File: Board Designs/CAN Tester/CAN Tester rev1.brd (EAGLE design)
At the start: 160 x 100 mm, 0 parts

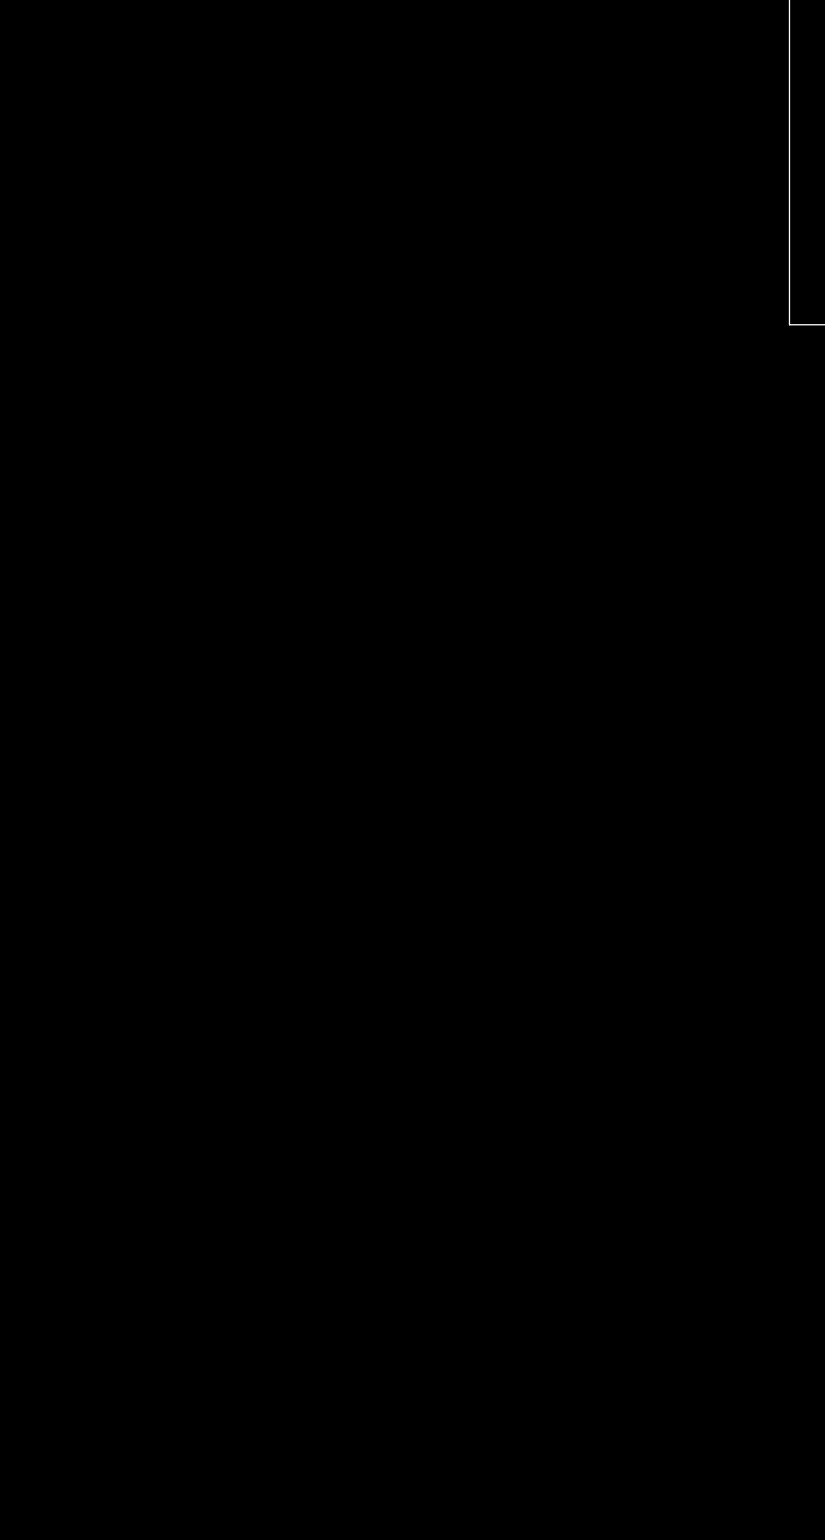
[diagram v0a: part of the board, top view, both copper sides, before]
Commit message: Added all parts to form can tester board
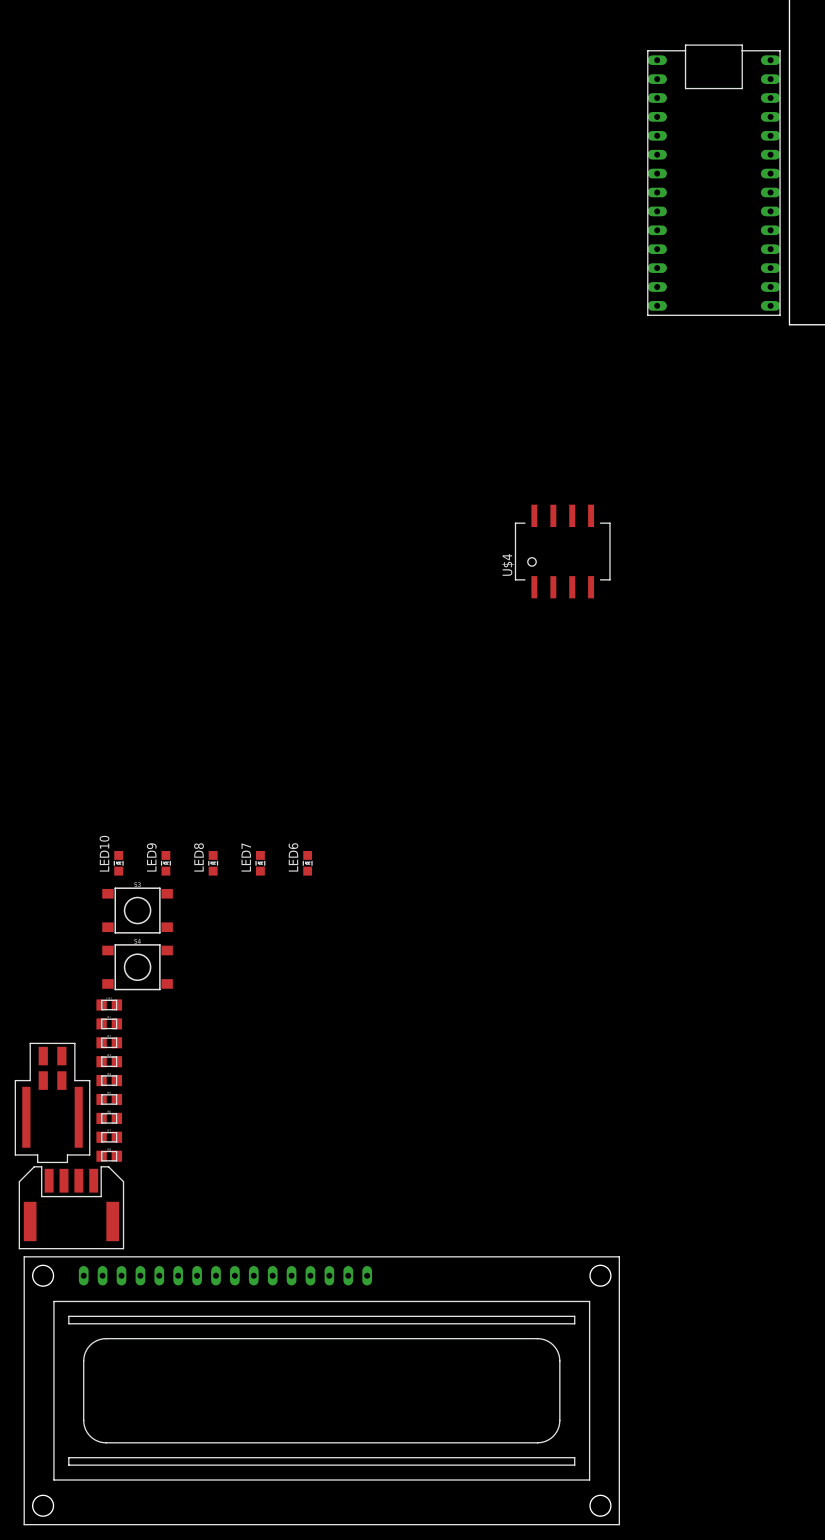
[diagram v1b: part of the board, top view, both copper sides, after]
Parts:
- added LED10, LED6, LED7, LED8, LED9: (no value), HyTechDevices:LED-805
- added R1: 120, HyTechDevices:0805
- added R2, R3, R4, R5, R6: 220, HyTechDevices:0805
- added R7, R8: 10K, HyTechDevices:0805
- added S3, S4: (no value), HyTechDevices:TACTILE_SWITCH_SMD_6.2MM_TALL
- added U$1: TEENSY_3.2_SIMPLE, HyTechDevices:TEENSY_3.2_SIMPLE
- added U$2: JUMPER, HyTechDevices:0805
- added U$4: ISO1050CAN, HyTechDevices:DUB8
- added X1: Minifit, HyTechDevices:DURACLIK_RIGHT_ANGLE-4
- added X2: HD44780LCD-1602, HyTechDevices:LCD1602
- added X3: Nanofit, HyTechDevices:NANO-FIT_RIGHT_ANGLE-4-SURFACE
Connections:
- new net N$1: R2.2, R3.1
- new net N$2: R3.2, R4.1
- new net N$3: LED10.A, R5.1

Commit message: increased component spacing
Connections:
- removed net N$1: R2.2, R3.1
- removed net N$2: R3.2, R4.1
- removed net N$3: LED10.A, R5.1
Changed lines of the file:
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@@
 </elements>
 <signals>
-<signal name="N$1">
-<contactref element="R2" pad="2"/>
-<contactref element="R3" pad="1"/>
-<wire x1="-90.415" y1="-96.52" x2="-92.465" y2="-99.06" width="0" layer="19" extent="1-1"/>
-</signal>
-<signal name="N$2">
-<contactref element="R3" pad="2"/>
-<contactref element="R4" pad="1"/>
-<wire x1="-90.415" y1="-99.06" x2="-92.465" y2="-101.6" width="0" layer="19" extent="1-1"/>
-</signal>
-<signal name="N$3">
-<contactref element="LED10" pad="A"/>
-<contactref element="R5" pad="1"/>
-<wire x1="-90.17" y1="-73.44" x2="-92.465" y2="-104.14" width="0" layer="19" extent="1-1"/>
-</signal>
 </signals>
 <mfgpreviewcolors>

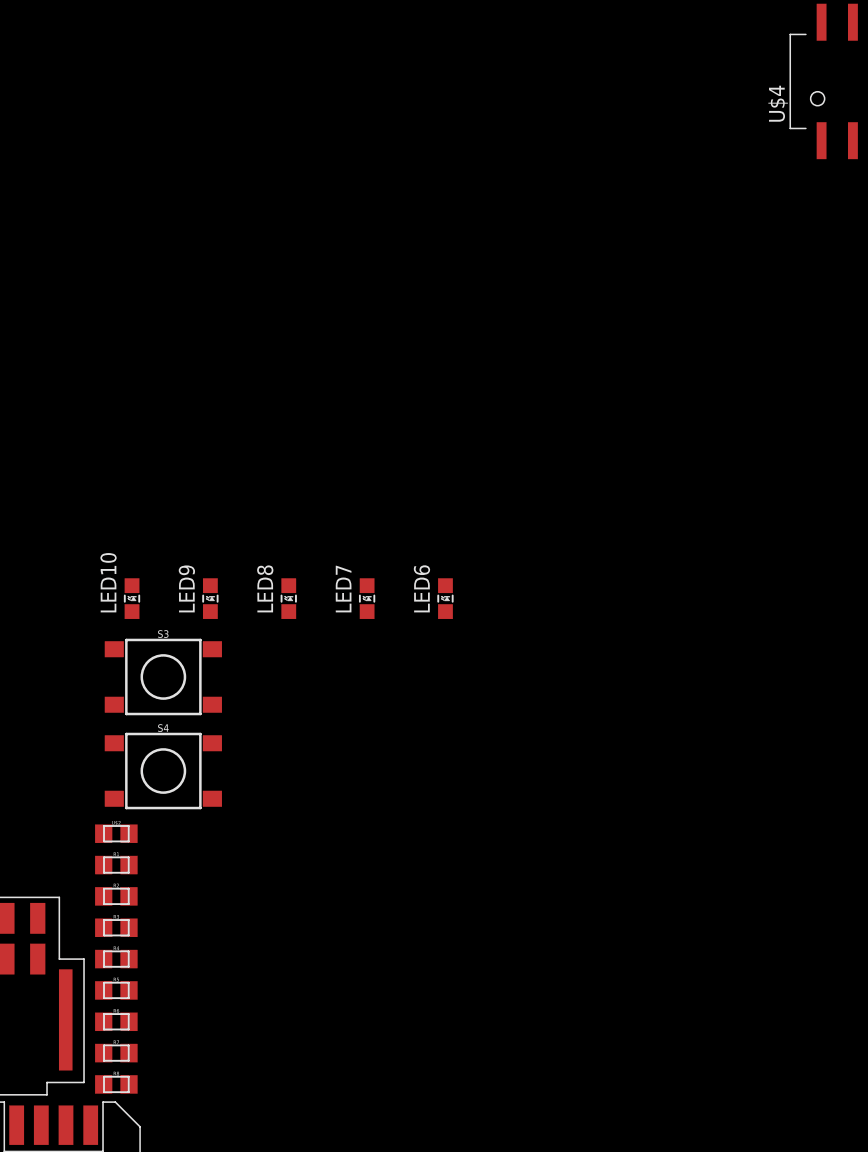
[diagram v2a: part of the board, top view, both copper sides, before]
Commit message: Labeled all componenets and organized them to make schematic later
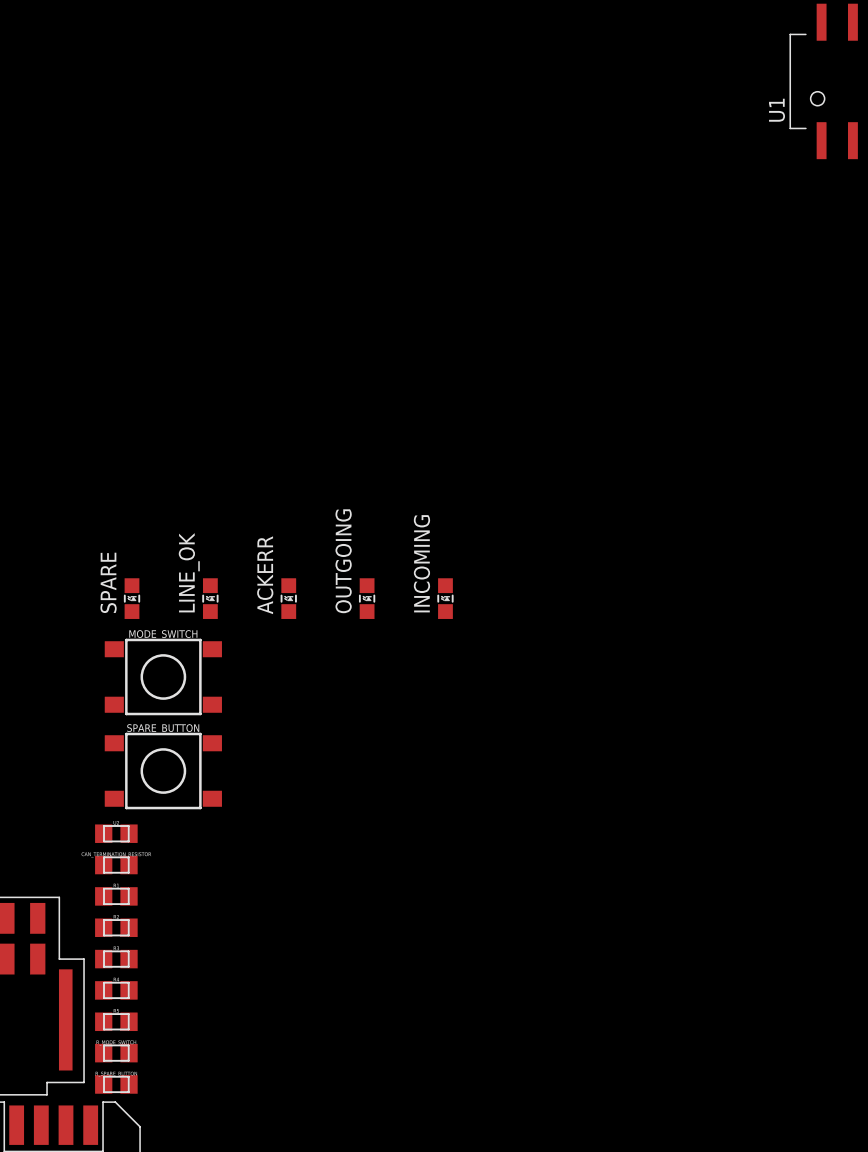
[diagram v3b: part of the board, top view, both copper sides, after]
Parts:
- removed R6: 220, HyTechDevices:0805
- added CAN_TERMINATION_RESISTOR: 120, HyTechDevices:0805
- ACKERR: value (none) -> RED
- INCOMING: value (none) -> YELLOW
- LINE_OK: value (none) -> GREEN
- OUTGOING: value (none) -> BLUE
- R1: value 120 -> 220
- SPARE: value (none) -> WHITE
- U1: value ISO1050CAN -> ISOLATED CAN TERMINAL
- U2: value JUMPER -> TERMINATION_RESISTOR_JUMPER
- U4: value HD44780LCD-1602 -> CHARACTER_LCD
- moved R2 2.54 mm to (-91.4, -99.1)
- moved R4 2.54 mm to (-91.4, -104.1)
- moved R5 2.54 mm to (-91.4, -106.7)
- moved R1 2.54 mm to (-91.4, -96.5)
- moved R3 2.54 mm to (-91.4, -101.6)
- renumbered LED10 to SPARE, LED6 to INCOMING, LED7 to OUTGOING, LED8 to ACKERR, LED9 to LINE_OK, R7 to R_MODE_SWITCH, R8 to R_SPARE_BUTTON, S3 to MODE_SWITCH, S4 to SPARE_BUTTON, U$1 to U3, U$2 to U2, U$4 to U1, X1 to M1, X2 to U4, X3 to M2
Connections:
- new net N$1: CAN_TERMINATION_RESISTOR.1, U2.2
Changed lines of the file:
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@@
 </autorouter>
 <elements>
-<element name="U$1" library="HyTechDevices" package="TEENSY_3.2_SIMPLE" value="TEENSY_3.2_SIMPLE" x="-19.05" y="1.27"/>
-<element name="U$4" library="HyTechDevices" package="DUB8" value="ISO1050CAN" x="-30.48" y="-30.48"/>
-<element name="LED6" library="HyTechDevices" package="LED-805" value="" x="-64.77" y="-72.39"/>
-<element name="LED7" library="HyTechDevices" package="LED-805" value="" x="-71.12" y="-72.39"/>
-<element name="LED8" library="HyTechDevices" package="LED-805" value="" x="-77.47" y="-72.39"/>
-<element name="LED9" library="HyTechDevices" package="LED-805" value="" x="-83.82" y="-72.39"/>
-<element name="LED10" library="HyTechDevices" package="LED-805" value="" x="-90.17" y="-72.39"/>
-<element name="S3" library="HyTechDevices" package="TACTILE_SWITCH_SMD_6.2MM_TALL" value="" x="-87.63" y="-78.74"/>
-<element name="S4" library="HyTechDevices" package="TACTILE_SWITCH_SMD_6.2MM_TALL" value="" x="-87.63" y="-86.36"/>
-<element name="U$2" library="HyTechDevices" package="0805" value="JUMPER" x="-91.44" y="-91.44"/>
-<element name="R1" library="HyTechDevices" package="0805" value="120" x="-91.44" y="-93.98"/>
-<element name="R2" library="HyTechDevices" package="0805" value="220" x="-91.44" y="-96.52"/>
-<element name="R3" library="HyTechDevices" package="0805" value="220" x="-91.44" y="-99.06"/>
-<element name="R4" library="HyTechDevices" package="0805" value="220" x="-91.44" y="-101.6"/>
-<element name="R5" library="HyTechDevices" package="0805" value="220" x="-91.44" y="-104.14"/>
-<element name="R6" library="HyTechDevices" package="0805" value="220" x="-91.44" y="-106.68"/>
-<element name="R7" library="HyTechDevices" package="0805" value="10K" x="-91.44" y="-109.22"/>
-<element name="R8" library="HyTechDevices" package="0805" value="10K" x="-91.44" y="-111.76"/>
-<element name="X3" library="HyTechDevices" package="NANO-FIT_RIGHT_ANGLE-4-SURFACE" value="Nanofit" x="-99.06" y="-101.6"/>
-<element name="X1" library="HyTechDevices" package="DURACLIK_RIGHT_ANGLE-4" value="Minifit" x="-96.52" y="-123.19"/>
-<element name="X2" library="HyTechDevices" package="LCD1602" value="HD44780LCD-1602" x="-102.87" y="-161.29"/>
+<element name="U3" library="HyTechDevices" package="TEENSY_3.2_SIMPLE" value="TEENSY_3.2_SIMPLE" x="-19.05" y="1.27"/>
+<element name="U1" library="HyTechDevices" package="DUB8" value="ISOLATED CAN TERMINAL" x="-30.48" y="-30.48"/>
+<element name="INCOMING" library="HyTechDevices" package="LED-805" value="YELLOW" x="-64.77" y="-72.39"/>
+<element name="OUTGOING" library="HyTechDevices" package="LED-805" value="BLUE" x="-71.12" y="-72.39"/>
+<element name="ACKERR" library="HyTechDevices" package="LED-805" value="RED" x="-77.47" y="-72.39"/>
+<element name="LINE_OK" library="HyTechDevices" package="LED-805" value="GREEN" x="-83.82" y="-72.39"/>
+<element name="SPARE" library="HyTechDevices" package="LED-805" value="WHITE" x="-90.17" y="-72.39"/>
+<element name="MODE_SWITCH" library="HyTechDevices" package="TACTILE_SWITCH_SMD_6.2MM_TALL" value="" x="-87.63" y="-78.74"/>
+<element name="SPARE_BUTTON" library="HyTechDevices" package="TACTILE_SWITCH_SMD_6.2MM_TALL" value="" x="-87.63" y="-86.36"/>
+<element name="U2" library="HyTechDevices" package="0805" value="TERMINATION_RESISTOR_JUMPER" x="-91.44" y="-91.44"/>
+<element name="CAN_TERMINATION_RESISTOR" library="HyTechDevices" package="0805" value="120" x="-91.44" y="-93.98"/>
+<element name="R1" library="HyTechDevices" package="0805" value="220" x="-91.44" y="-96.52"/>
+<element name="R2" library="HyTechDevices" package="0805" value="220" x="-91.44" y="-99.06"/>
+<element name="R3" library="HyTechDevices" package="0805" value="220" x="-91.44" y="-101.6"/>
+<element name="R4" library="HyTechDevices" package="0805" value="220" x="-91.44" y="-104.14"/>
+<element name="R5" library="HyTechDevices" package="0805" value="220" x="-91.44" y="-106.68"/>
+<element name="R_MODE_SWITCH" library="HyTechDevices" package="0805" value="10K" x="-91.44" y="-109.22"/>
+<element name="R_SPARE_BUTTON" library="HyTechDevices" package="0805" value="10K" x="-91.44" y="-111.76"/>
+<element name="M2" library="HyTechDevices" package="NANO-FIT_RIGHT_ANGLE-4-SURFACE" value="Nanofit" x="-99.06" y="-101.6"/>
+<element name="M1" library="HyTechDevices" package="DURACLIK_RIGHT_ANGLE-4" value="Minifit" x="-96.52" y="-123.19"/>
+<element name="U4" library="HyTechDevices" package="LCD1602" value="CHARACTER_LCD" x="-102.87" y="-161.29"/>
 </elements>
 <signals>
+<signal name="N$1">
+<contactref element="CAN_TERMINATION_RESISTOR" pad="1"/>
+<contactref element="U2" pad="2"/>
+<wire x1="-90.415" y1="-91.44" x2="-92.465" y2="-93.98" width="0" layer="19" extent="1-1"/>
+</signal>
 </signals>
 <mfgpreviewcolors>

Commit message: Adjusted resistor values to account for 3.3V teensy
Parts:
- R1, R2, R3, R4, R5: value 220 -> 55
- R_MODE_SWITCH, R_SPARE_BUTTON: value 10K -> 25K
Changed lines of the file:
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@@
 <element name="U2" library="HyTechDevices" package="0805" value="TERMINATION_RESISTOR_JUMPER" x="-91.44" y="-91.44"/>
 <element name="CAN_TERMINATION_RESISTOR" library="HyTechDevices" package="0805" value="120" x="-91.44" y="-93.98"/>
-<element name="R1" library="HyTechDevices" package="0805" value="220" x="-91.44" y="-96.52"/>
-<element name="R2" library="HyTechDevices" package="0805" value="220" x="-91.44" y="-99.06"/>
-<element name="R3" library="HyTechDevices" package="0805" value="220" x="-91.44" y="-101.6"/>
-<element name="R4" library="HyTechDevices" package="0805" value="220" x="-91.44" y="-104.14"/>
-<element name="R5" library="HyTechDevices" package="0805" value="220" x="-91.44" y="-106.68"/>
-<element name="R_MODE_SWITCH" library="HyTechDevices" package="0805" value="10K" x="-91.44" y="-109.22"/>
-<element name="R_SPARE_BUTTON" library="HyTechDevices" package="0805" value="10K" x="-91.44" y="-111.76"/>
+<element name="R1" library="HyTechDevices" package="0805" value="55" x="-91.44" y="-96.52"/>
+<element name="R2" library="HyTechDevices" package="0805" value="55" x="-91.44" y="-99.06"/>
+<element name="R3" library="HyTechDevices" package="0805" value="55" x="-91.44" y="-101.6"/>
+<element name="R4" library="HyTechDevices" package="0805" value="55" x="-91.44" y="-104.14"/>
+<element name="R5" library="HyTechDevices" package="0805" value="55" x="-91.44" y="-106.68"/>
+<element name="R_MODE_SWITCH" library="HyTechDevices" package="0805" value="25K" x="-91.44" y="-109.22"/>
+<element name="R_SPARE_BUTTON" library="HyTechDevices" package="0805" value="25K" x="-91.44" y="-111.76"/>
 <element name="M2" library="HyTechDevices" package="NANO-FIT_RIGHT_ANGLE-4-SURFACE" value="Nanofit" x="-99.06" y="-101.6"/>
 <element name="M1" library="HyTechDevices" package="DURACLIK_RIGHT_ANGLE-4" value="Minifit" x="-96.52" y="-123.19"/>
